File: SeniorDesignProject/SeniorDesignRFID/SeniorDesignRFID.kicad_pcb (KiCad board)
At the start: 2 copper layers, 6 parts, among them J1 CONN_01X05

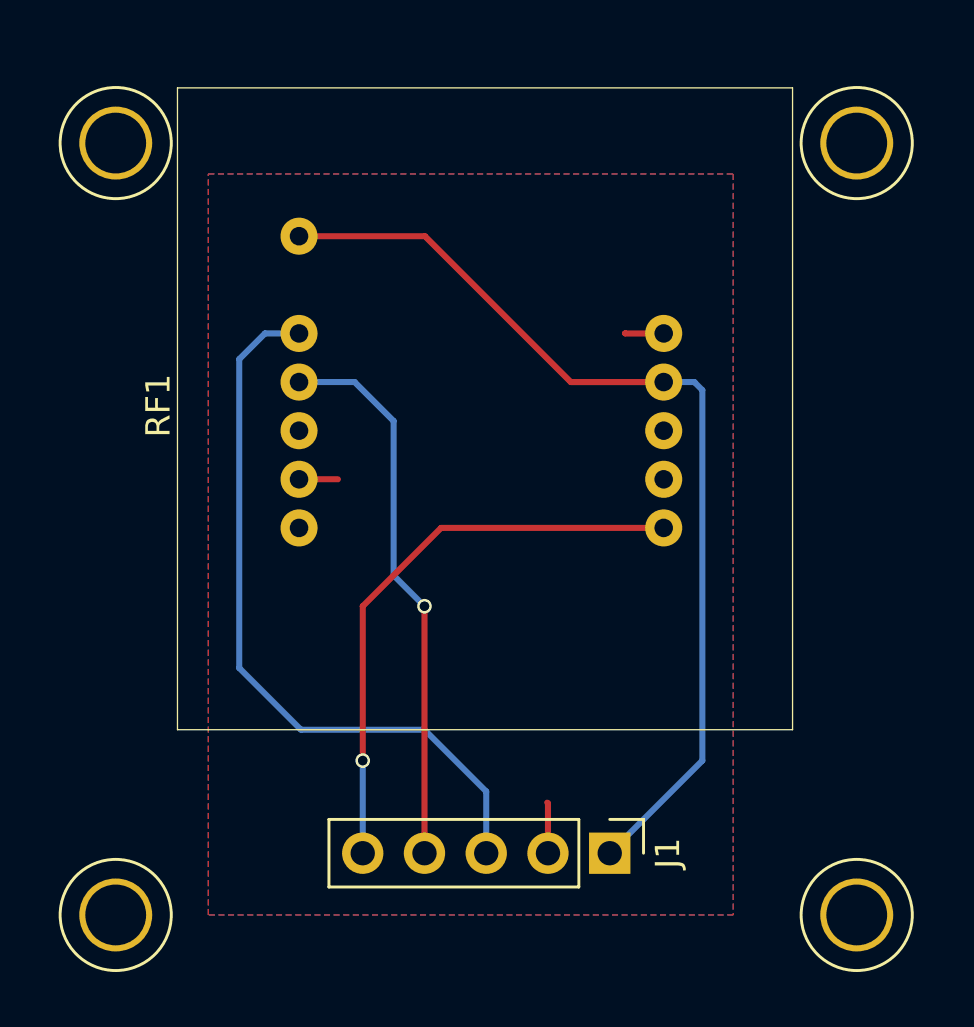
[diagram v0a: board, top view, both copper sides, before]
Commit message: Updated RFID board with silk screen labels and moved some traces, Bothom copper poor not showing though...
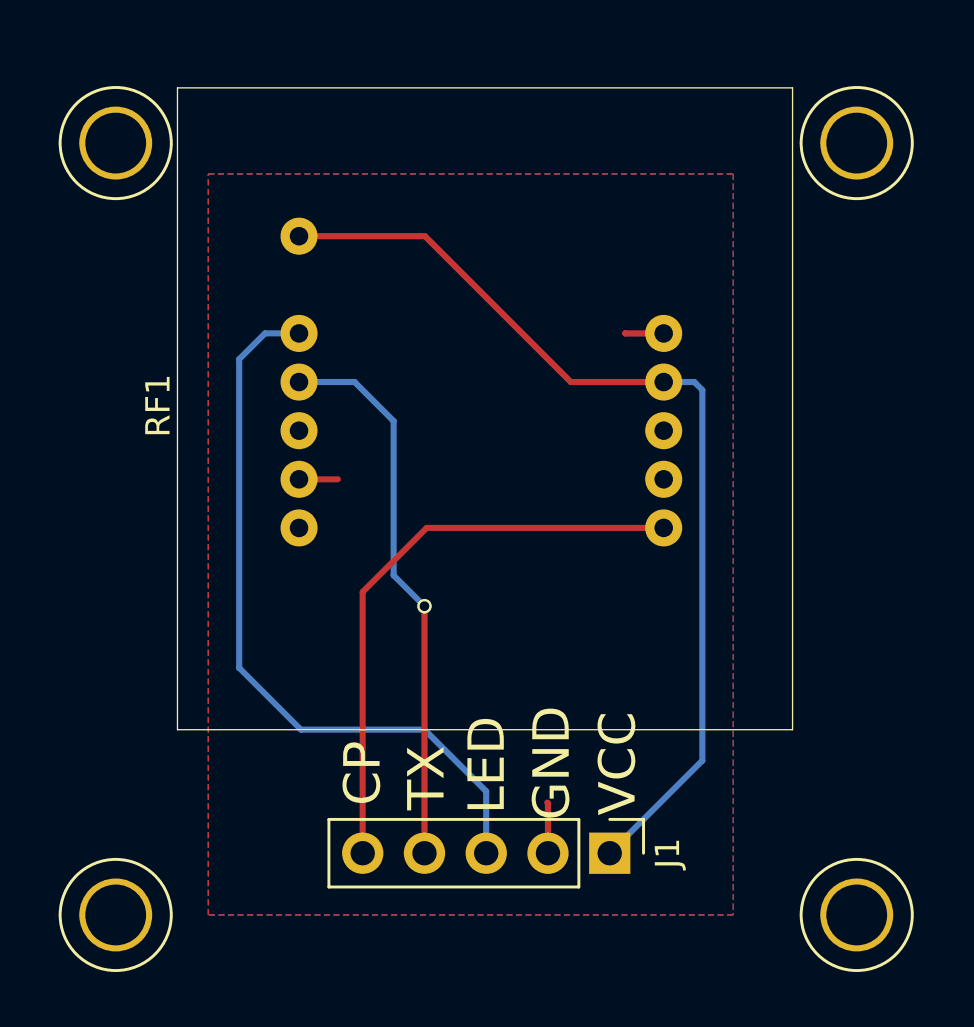
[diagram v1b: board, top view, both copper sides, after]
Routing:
- net Net-(J1-Pad5): track 23.9 -> 24.2 mm, vias 1 -> 0
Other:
- board text added: "CP"
- board text added: "GND"
- board text added: "LED"
- board text added: "TX"
- board text added: "VCC"
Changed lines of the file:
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@@
     (area 177.514999 105.197 213.645001 145.045)
     (thickness 1.6)
-    (drawings 9)
-    (tracks 30)
+    (drawings 14)
+    (tracks 28)
     (zones 0)
     (modules 6)
@@
     )
   )
+  (gr_text CP (at 190.5 135.14 90) (layer F.SilkS)
+    (effects (font (size 1.5 1.5) (thickness 0.3)))
+  )
+  (gr_text TX (at 193.13 135.33 90) (layer F.SilkS)
+    (effects (font (size 1.5 1.5) (thickness 0.3)))
+  )
+  (gr_text LED (at 195.61 134.8 90) (layer F.SilkS)
+    (effects (font (size 1.5 1.5) (thickness 0.3)))
+  )
+  (gr_text GND (at 198.28 134.72 90) (layer F.SilkS)
+    (effects (font (size 1.5 1.5) (thickness 0.3)))
+  )
+  (gr_text VCC (at 200.99 134.74 90) (layer F.SilkS)
+    (effects (font (size 1.5 1.5) (thickness 0.3)))
+  )
   (gr_line (start 177.8 143.51) (end 177.8 140.97) (angle 90) (layer Dwgs.User) (width 0.2))
   (gr_line (start 213.36 143.51) (end 177.8 143.51) (angle 90) (layer Dwgs.User) (width 0.2))
@@
   (segment (start 204.47 119.38) (end 204.47 134.62) (width 0.25) (layer B.Cu) (net 1))
   (segment (start 204.14 119.05) (end 204.47 119.38) (width 0.25) (layer B.Cu) (net 1))
-  (segment (start 198.12 138.43) (end 198.12 136.38) (width 0.25) (layer F.Cu) (net 2) (status 400000))
-  (segment (start 198.12 136.38) (end 198.09 136.35) (width 0.25) (layer F.Cu) (net 2))
   (segment (start 187.88 123.05) (end 189.48 123.05) (width 0.25) (layer F.Cu) (net 2))
   (segment (start 202.88 117.05) (end 201.3 117.05) (width 0.25) (layer F.Cu) (net 2))
   (segment (start 201.3 117.05) (end 201.29 117.04) (width 0.25) (layer F.Cu) (net 2))
+  (segment (start 198.12 138.43) (end 198.12 136.38) (width 0.25) (layer F.Cu) (net 2))
+  (segment (start 198.12 136.38) (end 198.09 136.35) (width 0.25) (layer F.Cu) (net 2))
   (segment (start 187.88 117.05) (end 186.48 117.05) (width 0.25) (layer B.Cu) (net 3))
   (segment (start 195.58 135.89) (end 195.58 138.43) (width 0.25) (layer B.Cu) (net 3))
@@
   (segment (start 193.04 128.27) (end 191.77 127) (width 0.25) (layer B.Cu) (net 4))
   (via (at 193.04 128.27) (size 0.6) (drill 0.4) (layers F.Cu B.Cu) (net 4))
-  (segment (start 190.5 138.43) (end 190.5 134.62) (width 0.25) (layer B.Cu) (net 5))
-  (segment (start 193.72 125.05) (end 202.88 125.05) (width 0.25) (layer F.Cu) (net 5))
-  (segment (start 190.5 128.27) (end 193.72 125.05) (width 0.25) (layer F.Cu) (net 5))
-  (segment (start 190.5 134.62) (end 190.5 128.27) (width 0.25) (layer F.Cu) (net 5))
-  (via (at 190.5 134.62) (size 0.6) (drill 0.4) (layers F.Cu B.Cu) (net 5))
+  (segment (start 193.13 125.05) (end 202.88 125.05) (width 0.25) (layer F.Cu) (net 5))
+  (segment (start 190.5 127.68) (end 193.13 125.05) (width 0.25) (layer F.Cu) (net 5))
+  (segment (start 190.5 138.43) (end 190.5 127.68) (width 0.25) (layer F.Cu) (net 5))
   (zone (net 2) (net_name "Net-(J1-Pad2)") (layer B.Cu) (hatch edge 0.508)
     (connect_pads no (clearance 0.508))

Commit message: Added silk screen and gerber files for osh park fabrication
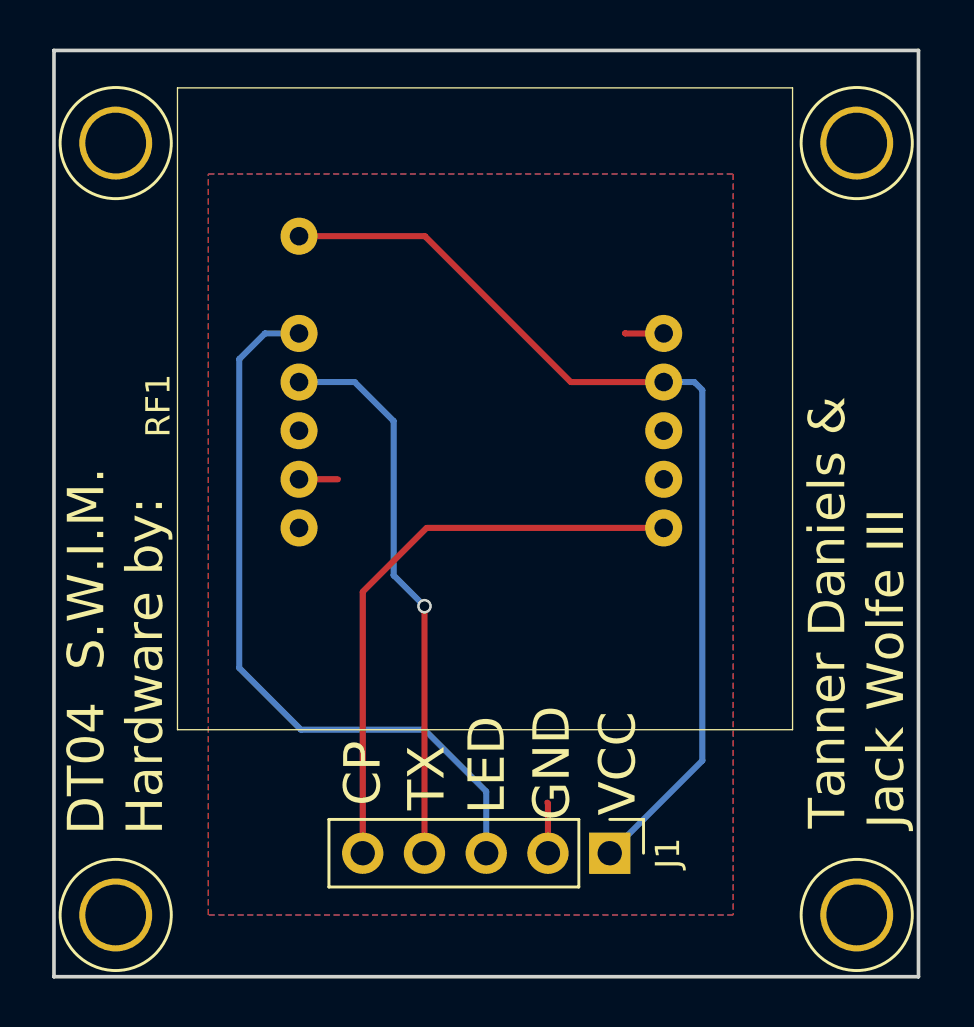
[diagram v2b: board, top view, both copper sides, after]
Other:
- board outline added: 35.6 x 38.1 mm
- board text added: "DT04 S.W.I.M. Hardware by:"
- board text added: "Tanner Daniels & Jack Wolfe III"
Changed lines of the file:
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@@
     (area 177.514999 105.197 213.645001 145.045)
     (thickness 1.6)
-    (drawings 14)
+    (drawings 20)
     (tracks 28)
     (zones 0)
@@
     (visible_elements FFFFFF7F)
     (pcbplotparams
-      (layerselection 0x00030_80000001)
+      (layerselection 0x01020_80000001)
       (usegerberextensions false)
       (excludeedgelayer true)
@@
       (outputformat 1)
       (mirror false)
-      (drillshape 1)
+      (drillshape 0)
       (scaleselection 1)
       (outputdirectory ""))
@@
     )
   )
+  (gr_line (start 177.8 143.51) (end 177.8 105.41) (angle 90) (layer Edge.Cuts) (width 0.15))
+  (gr_line (start 213.36 143.51) (end 177.8 143.51) (angle 90) (layer Edge.Cuts) (width 0.15))
+  (gr_line (start 213.36 105.41) (end 213.36 143.51) (angle 90) (layer Edge.Cuts) (width 0.15))
+  (gr_line (start 177.8 105.41) (end 213.36 105.41) (angle 90) (layer Edge.Cuts) (width 0.15))
+  (gr_text "Tanner Daniels &\nJack Wolfe III" (at 210.82 137.414 90) (layer F.SilkS)
+    (effects (font (size 1.5 1.5) (thickness 0.1)) (justify left))
+  )
+  (gr_text "DT04  S.W.I.M.\nHardware by:" (at 180.34 137.668 90) (layer F.SilkS)
+    (effects (font (size 1.5 1.5) (thickness 0.1)) (justify left))
+  )
   (gr_text CP (at 190.5 135.14 90) (layer F.SilkS)
